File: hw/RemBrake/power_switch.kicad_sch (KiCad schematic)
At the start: 42 parts, among them Q1 SiS415DNT, Q2 BC337, Q3 BC847, Q4 BC337, Q5 BC847, U1 TPS62140, U2 BD48ExxG, U3 XC6220B331MR, U4 MAX40200AUK

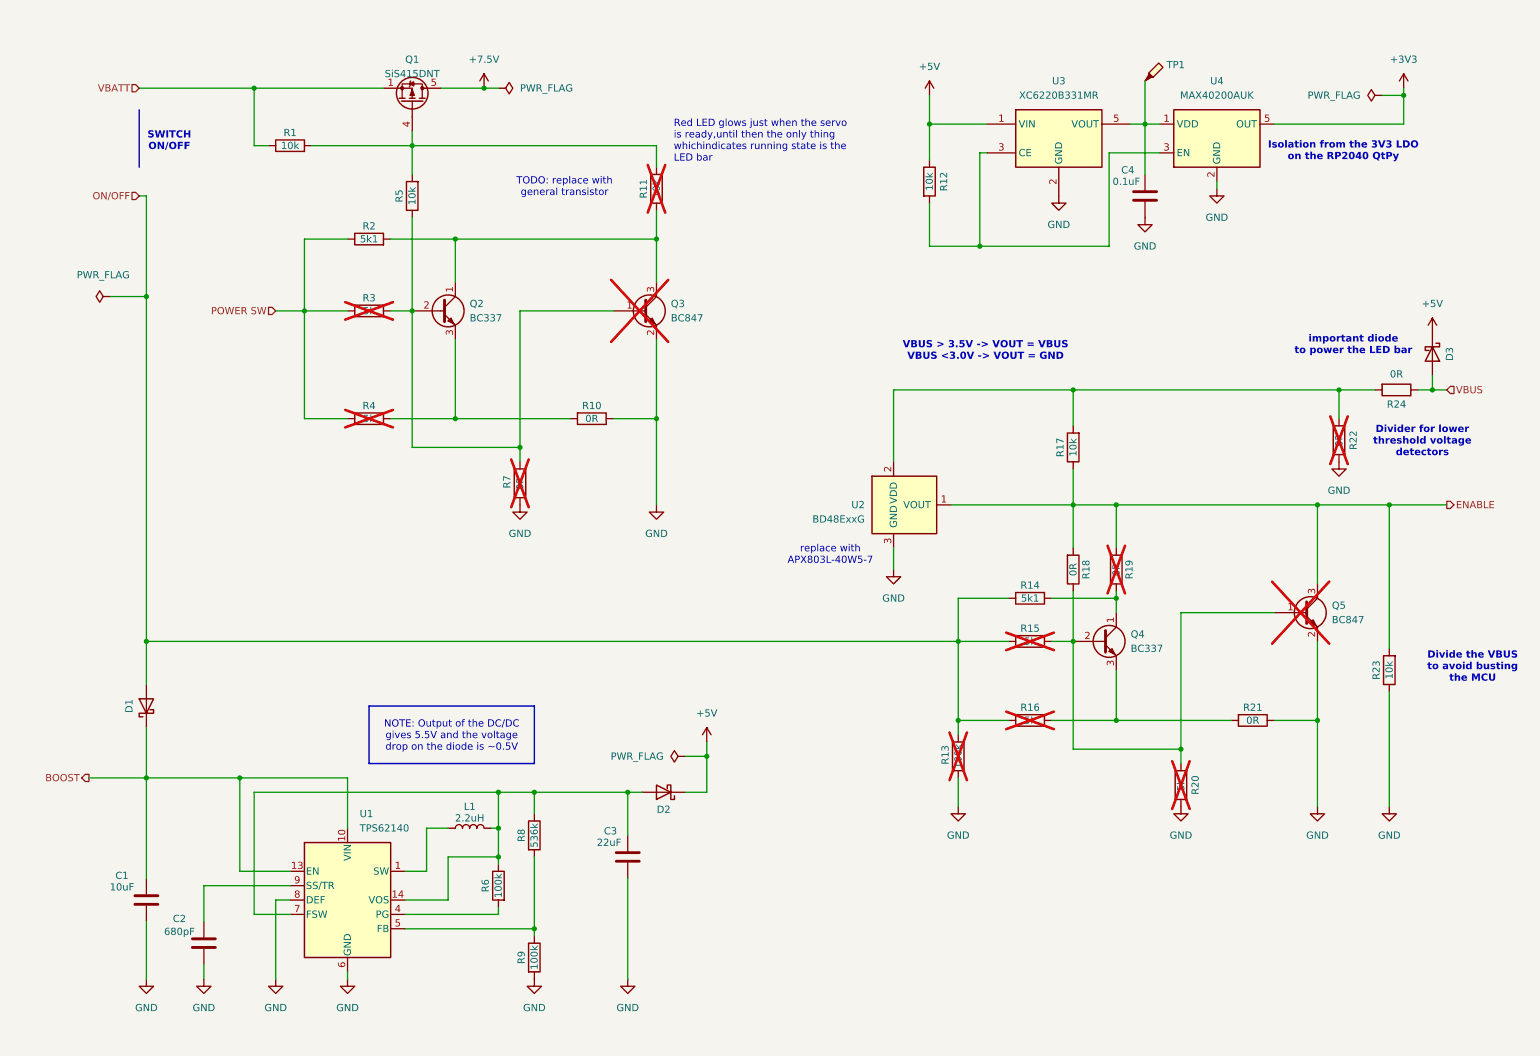
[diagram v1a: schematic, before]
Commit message: added diodes to connect voltages to display and remote button even when connected to charger
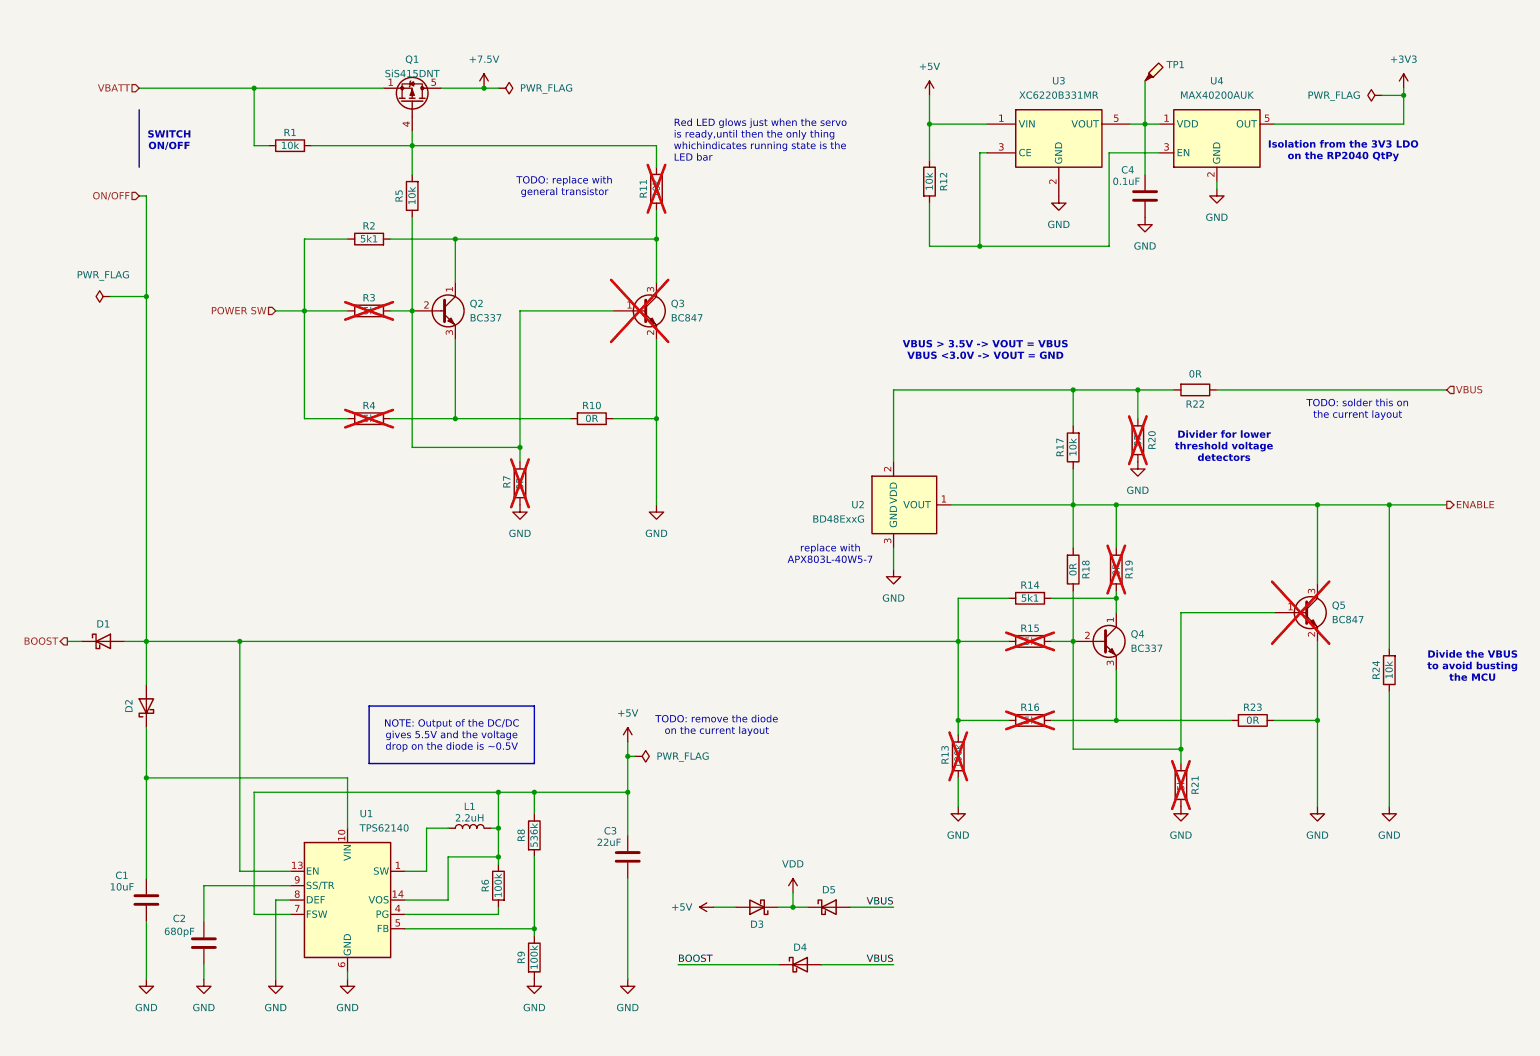
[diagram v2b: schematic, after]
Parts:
- added D1, D4: MBR0520, Diode_SMD:D_SOD-123, symbol Device:D_Schottky
- renumbered D1 to D2, D2 to D3, D3 to D5, R22 to R20, R20 to R21, R24 to R22, R21 to R23, R23 to R24
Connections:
- net +5V: now also C3.1, D3.2 (A), L1.2, R6.1, R8.1, U1.14 (VOS), U1.7 (FSW); no longer D3.1 (K), D5.1 (K)
- net BOOST: now also D1.1 (K), D4.1 (K); no longer C1.1, D2.1 (K), U1.10 (VIN), U1.11 (VIN), U1.12 (VIN), U1.13 (EN)
- net ON/OFF: now also U1.13 (EN), D1.2 (A)
- net VBUS: now also D4.2 (A)
- new net: C1.1, D2.1 (K), U1.10 (VIN), U1.11 (VIN), U1.12 (VIN)
- new net VDD: D3.1 (K), D5.1 (K)
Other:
- note added: "TODO: remove the diode on the current layout"
- note added: "TODO: solder this on the current layout"
- note removed: "important diode to power the LED bar"
- moved on the sheet: D3, D5, R20, R22

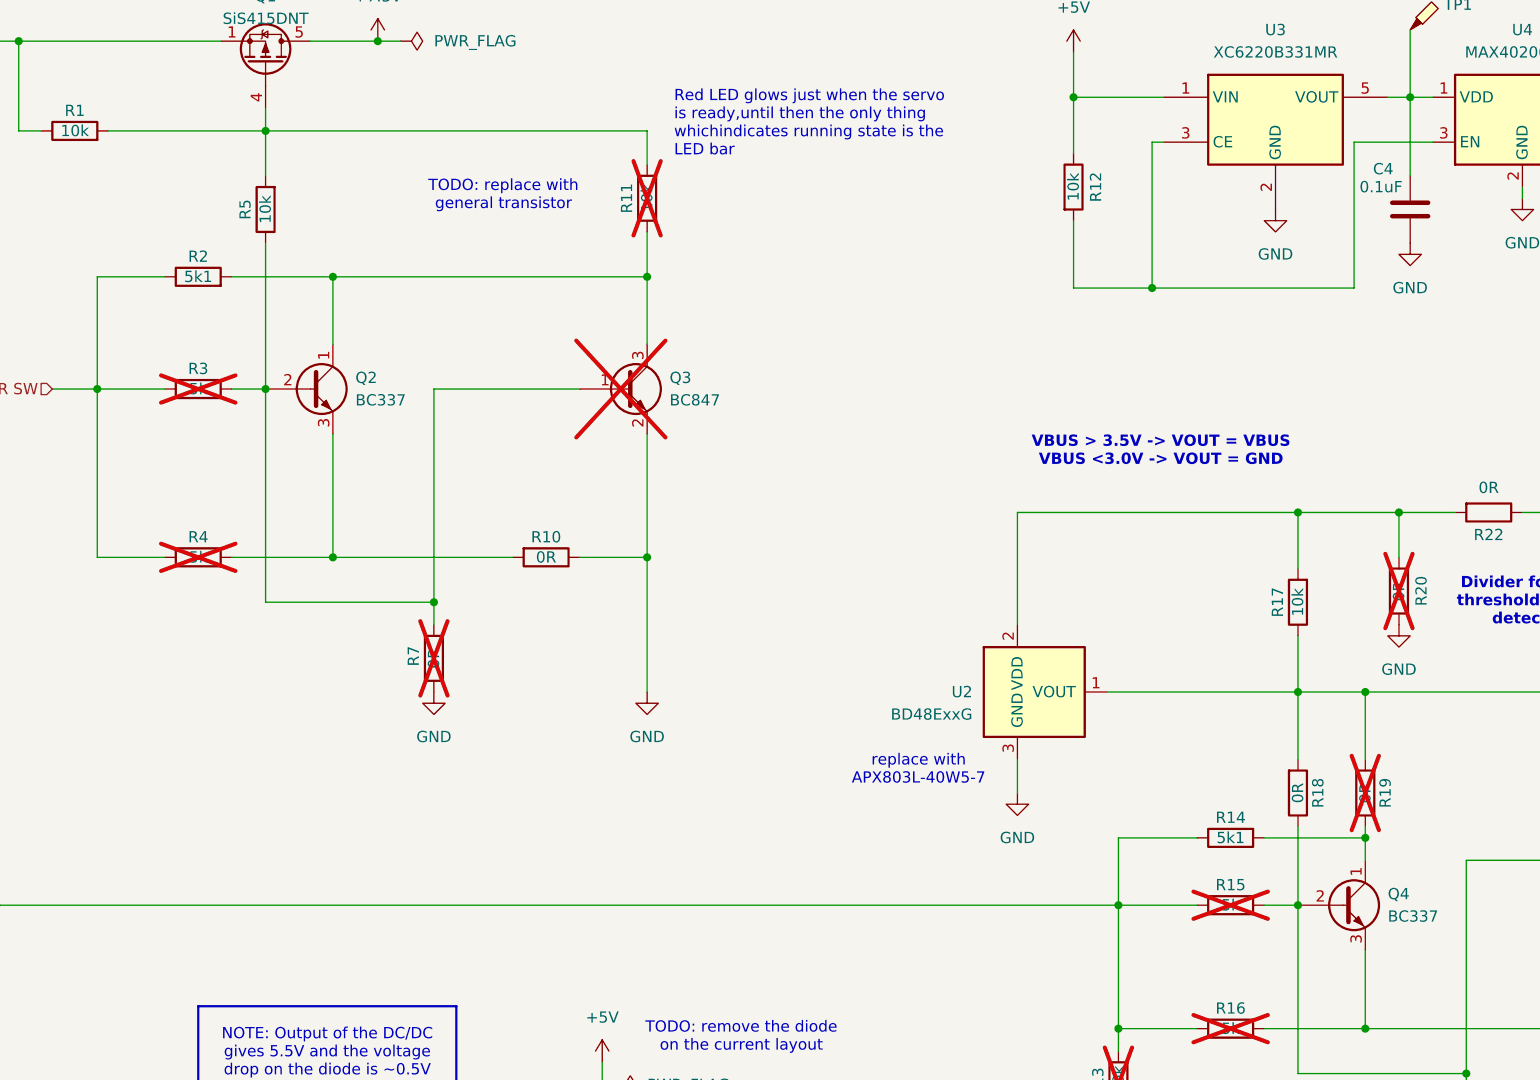
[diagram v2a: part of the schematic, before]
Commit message: adjusted connections to be able to use bc337
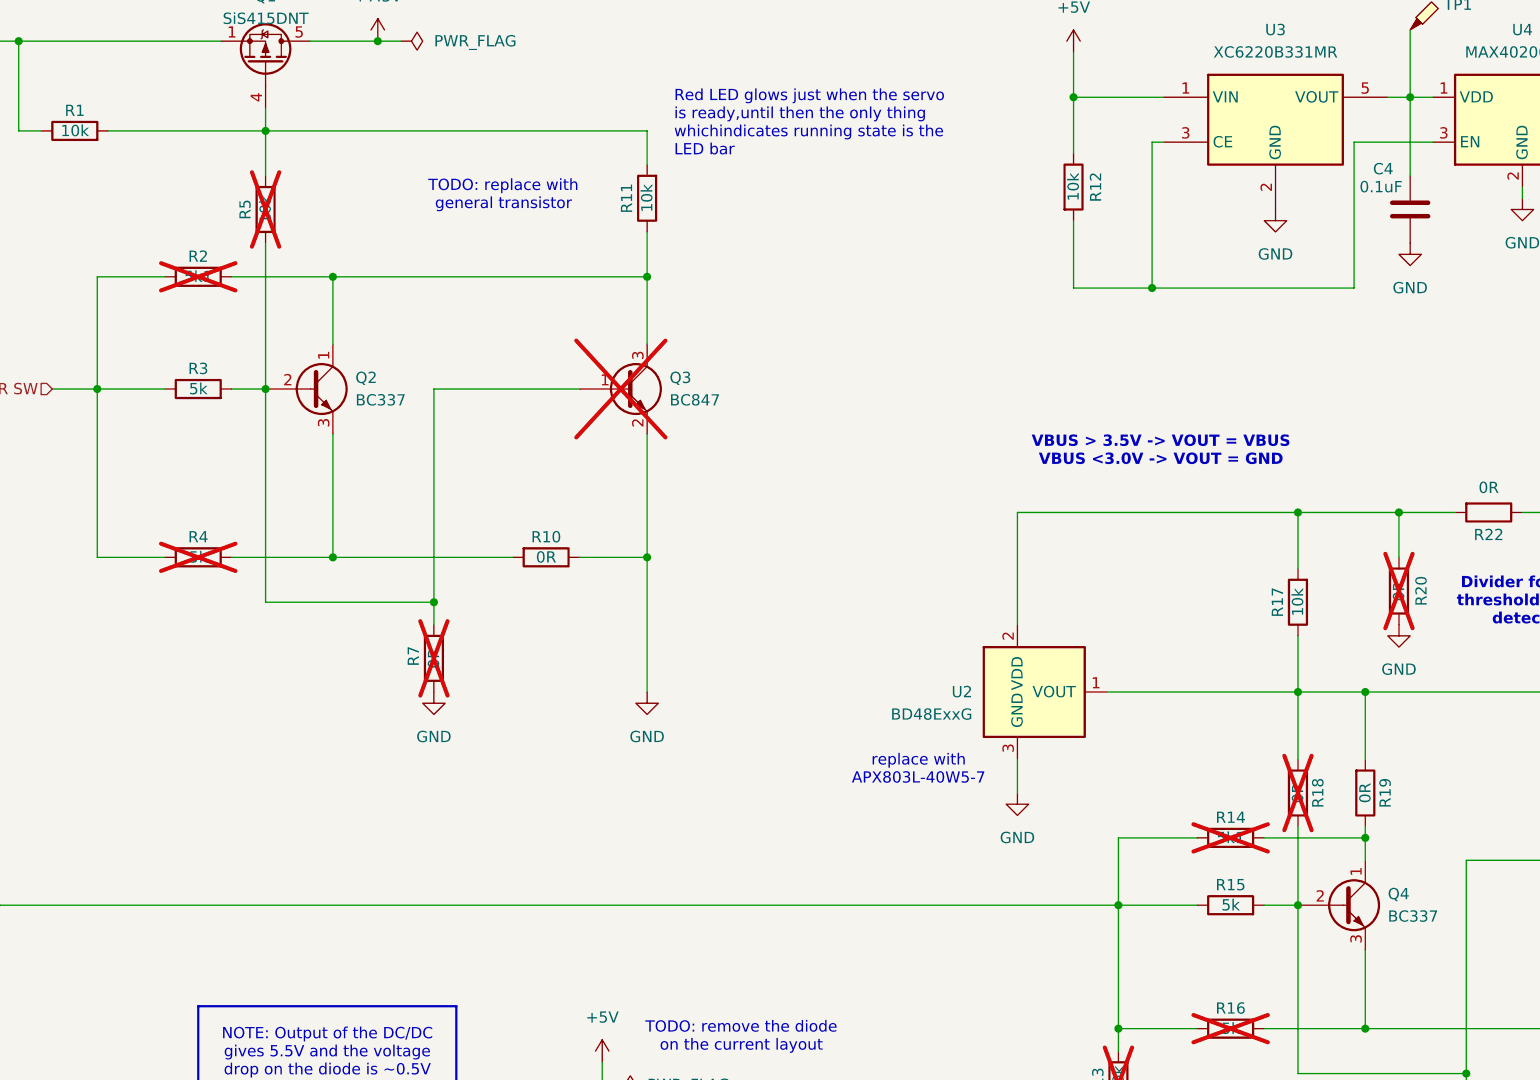
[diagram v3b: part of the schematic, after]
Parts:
- R11, R15, R19: now fitted; now in the parts list
- R14, R18, R2, R5: now not fitted; now left out of the parts list
- R3: now fitted
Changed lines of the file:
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@@
 (kicad_sch
-	(version 20250318)
+	(version 20250513)
 	(generator "eeschema")
 	(generator_version "9.99")
@@
 		(unit 1)
 		(exclude_from_sim no)
-		(in_bom yes)
+		(in_bom no)
 		(on_board yes)
-		(dnp no)
+		(dnp yes)
 		(property "Reference" "R14"
 			(at 194.31 114.554 90)
@@
 		(unit 1)
 		(exclude_from_sim no)
-		(in_bom yes)
+		(in_bom no)
 		(on_board yes)
-		(dnp no)
+		(dnp yes)
 		(property "Reference" "R18"
 			(at 204.216 111.76 90)
@@
 		(on_board yes)
 		(dnp no)
-		(property "Purchase" "https://cz.farnell.com/diodes-inc/mbr230s1f-7/schottky-rectifier-30v-2a-sod/dp/3405045"
-			(at 153.67 181.61 0)
-			(hide yes)
-			(effects
-				(font
-					(size 1.27 1.27)
-				)
-			)
-		)
 		(property "Reference" "D4"
 			(at 153.67 178.562 0)
@@
 			)
 		)
+		(property "Purchase" "https://cz.farnell.com/diodes-inc/mbr230s1f-7/schottky-rectifier-30v-2a-sod/dp/3405045"
+			(at 153.67 181.61 0)
+			(hide yes)
+			(effects
+				(font
+					(size 1.27 1.27)
+				)
+			)
+		)
 		(pin "1"
 		)
@@
 		(unit 1)
 		(exclude_from_sim no)
-		(in_bom no)
+		(in_bom yes)
 		(on_board yes)
-		(dnp yes)
+		(dnp no)
 		(property "Reference" "R15"
 			(at 194.31 122.174 90)
@@
 		(on_board yes)
 		(dnp no)
-		(property "Purchase" "https://cz.farnell.com/murata/dfe252012p-2r2m-p2/inductor-2-2uh-20-2-6a-shld-1008/dp/2530074"
-			(at 95.25 157.48 90)
-			(hide yes)
-			(effects
-				(font
-					(size 1.27 1.27)
-				)
-			)
-		)
 		(property "Reference" "L1"
 			(at 95.25 153.67 90)
@@
 			)
 		)
+		(property "Purchase" "https://cz.farnell.com/murata/dfe252012p-2r2m-p2/inductor-2-2uh-20-2-6a-shld-1008/dp/2530074"
+			(at 95.25 157.48 90)
+			(hide yes)
+			(effects
+				(font
+					(size 1.27 1.27)
+				)
+			)
+		)
 		(pin "2"
 		)
@@
 		(on_board yes)
 		(dnp no)
-		(property "Purchase" "https://cz.farnell.com/diodes-inc/mbr230s1f-7/schottky-rectifier-30v-2a-sod/dp/3405045"
-			(at 38.1 135.89 0)
-			(hide yes)
-			(effects
-				(font
-					(size 1.27 1.27)
-				)
-			)
-		)
 		(property "Reference" "D2"
 			(at 35.052 135.89 0)
@@
 			)
 		)
+		(property "Purchase" "https://cz.farnell.com/diodes-inc/mbr230s1f-7/schottky-rectifier-30v-2a-sod/dp/3405045"
+			(at 38.1 135.89 0)
+			(hide yes)
+			(effects
+				(font
+					(size 1.27 1.27)
+				)
+			)
+		)
 		(pin "1"
 		)
@@
 		(unit 1)
 		(exclude_from_sim no)
-		(in_bom no)
+		(in_bom yes)
 		(on_board yes)
-		(dnp yes)
+		(dnp no)
 		(property "Reference" "R19"
 			(at 211.836 111.76 90)
@@
 		(in_bom no)
 		(on_board yes)
-		(dnp yes)
+		(dnp no)
 		(property "Reference" "R3"
 			(at 77.47 63.754 90)
@@
 		(unit 1)
 		(exclude_from_sim no)
-		(in_bom no)
+		(in_bom yes)
 		(on_board yes)
-		(dnp yes)
+		(dnp no)
 		(property "Reference" "R11"
 			(at 125.984 44.45 90)
@@
 		(unit 1)
 		(exclude_from_sim no)
-		(in_bom yes)
+		(in_bom no)
 		(on_board yes)
-		(dnp no)
+		(dnp yes)
 		(property "Reference" "R2"
 			(at 77.47 51.054 90)
@@
 		(on_board yes)
 		(dnp no)
-		(property "Purchase" "https://cz.farnell.com/diodes-inc/mbr230s1f-7/schottky-rectifier-30v-2a-sod/dp/3405045"
-			(at 30.48 124.46 0)
-			(hide yes)
-			(effects
-				(font
-					(size 1.27 1.27)
-				)
-			)
-		)
 		(property "Reference" "D1"
 			(at 30.48 121.412 0)
@@
 			)
 		)
+		(property "Purchase" "https://cz.farnell.com/diodes-inc/mbr230s1f-7/schottky-rectifier-30v-2a-sod/dp/3405045"
+			(at 30.48 124.46 0)
+			(hide yes)
+			(effects
+				(font
+					(size 1.27 1.27)
+				)
+			)
+		)
 		(pin "1"
 		)
@@
 		(on_board yes)
 		(dnp no)
-		(property "Purchase" "https://cz.farnell.com/diodes-inc/mbr230s1f-7/schottky-rectifier-30v-2a-sod/dp/3405045"
-			(at 146.05 171.45 0)
-			(hide yes)
-			(effects
-				(font
-					(size 1.27 1.27)
-				)
-			)
-		)
 		(property "Reference" "D3"
 			(at 146.05 174.498 0)
@@
 			)
 		)
+		(property "Purchase" "https://cz.farnell.com/diodes-inc/mbr230s1f-7/schottky-rectifier-30v-2a-sod/dp/3405045"
+			(at 146.05 171.45 0)
+			(hide yes)
+			(effects
+				(font
+					(size 1.27 1.27)
+				)
+			)
+		)
 		(pin "1"
 		)
@@
 		(on_board yes)
 		(dnp no)
-		(property "Purchase" "https://cz.farnell.com/diodes-inc/mbr230s1f-7/schottky-rectifier-30v-2a-sod/dp/3405045"
-			(at 158.75 171.45 0)
-			(hide yes)
-			(effects
-				(font
-					(size 1.27 1.27)
-				)
-			)
-		)
 		(property "Reference" "D5"
 			(at 158.75 168.402 0)
@@
 			)
 		)
+		(property "Purchase" "https://cz.farnell.com/diodes-inc/mbr230s1f-7/schottky-rectifier-30v-2a-sod/dp/3405045"
+			(at 158.75 171.45 0)
+			(hide yes)
+			(effects
+				(font
+					(size 1.27 1.27)
+				)
+			)
+		)
 		(pin "1"
 		)
@@
 		(unit 1)
 		(exclude_from_sim no)
-		(in_bom yes)
+		(in_bom no)
 		(on_board yes)
-		(dnp no)
+		(dnp yes)
 		(property "Reference" "R5"
 			(at 82.804 45.72 90)
